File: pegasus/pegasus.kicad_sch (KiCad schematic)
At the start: 11 parts, among them IC1 Adafruit_MPL3115A2, IC2 Adafruit-BNO055-PCB, IC3 L70B-M39, IC4 RFD900, J1 Conn_01x02_Female, J2 Conn_01x02_Female, J3 Conn_01x02_Female, J4 Conn_Coaxial, J5 Conn_Coaxial, U1 Teensy4.1, U2 L7805

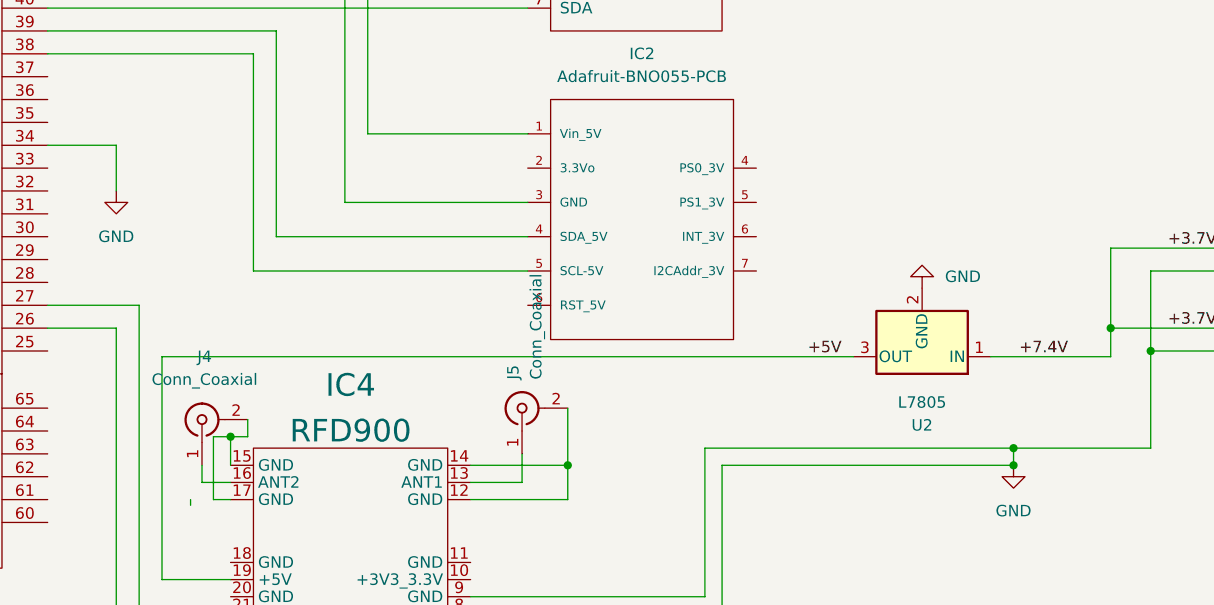
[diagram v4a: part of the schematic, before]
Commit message: added voltage regulator to schematic and pcb
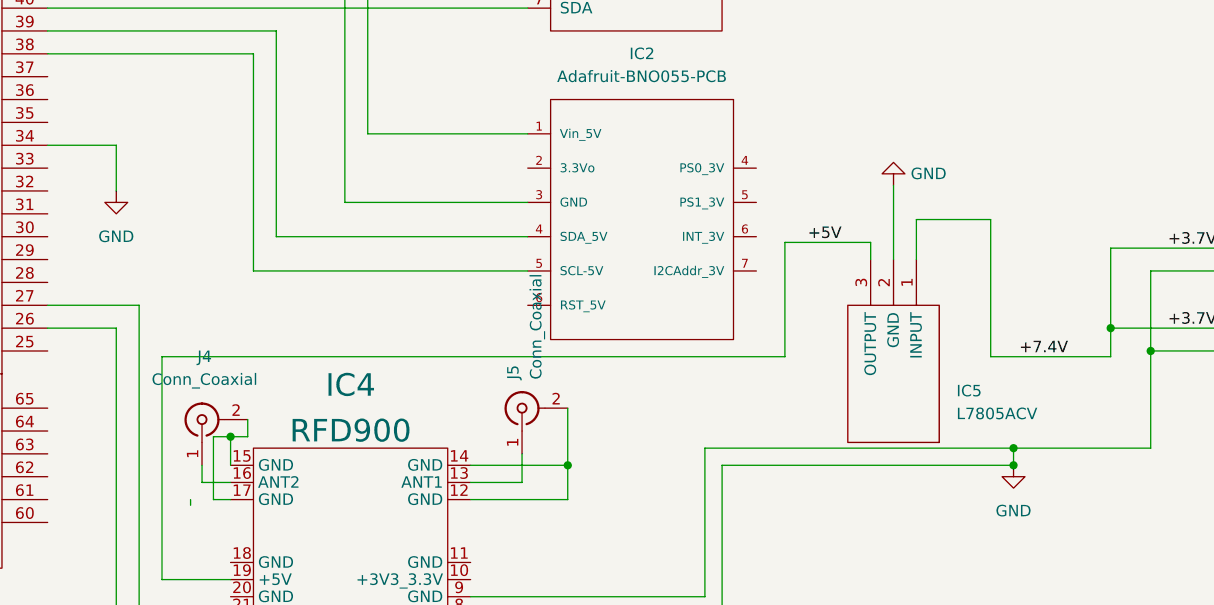
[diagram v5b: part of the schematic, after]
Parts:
- removed U2: L7805, symbol Regulator_Linear:L7805
- added IC5: L7805ACV, TO255P460X1020X2008-3P, symbol Voltage Regulator:L7805ACV
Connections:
- net +3.7V: now also IC5.1 (INPUT)
- net +5V: now also IC5.3 (OUTPUT)
- net GND: now also IC5.2 (GND)
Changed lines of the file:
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@@
   (junction (at 57.785 35.56) (diameter 0) (color 0 0 0 0)
   )
+  (wire (pts (xy 179.705 150.495) (xy 110.49 150.495))
+    (stroke (width 0) (type default) (color 0 0 0 0))
+  )
   (wire (pts (xy 105.41 127) (xy 105.41 132.08))
     (stroke (width 0) (type default) (color 0 0 0 0))
@@
     (stroke (width 0) (type default) (color 0 0 0 0))
   )
-  (wire (pts (xy 187.325 150.495) (xy 110.49 150.495))
-    (stroke (width 0) (type default) (color 0 0 0 0))
-  )
   (wire (pts (xy 228.6 147.32) (xy 215.9 147.32))
     (stroke (width 0) (type default) (color 0 0 0 0))
@@
     (stroke (width 0) (type default) (color 0 0 0 0))
   )
+  (wire (pts (xy 189.23 137.795) (xy 179.705 137.795))
+    (stroke (width 0) (type default) (color 0 0 0 0))
+  )
+  (wire (pts (xy 179.705 137.795) (xy 179.705 150.495))
+    (stroke (width 0) (type default) (color 0 0 0 0))
+  )
   (wire (pts (xy 220.345 140.97) (xy 220.345 149.86))
     (stroke (width 0) (type default) (color 0 0 0 0))
@@
     (stroke (width 0) (type default) (color 0 0 0 0))
   )
+  (wire (pts (xy 202.565 135.255) (xy 194.31 135.255))
+    (stroke (width 0) (type default) (color 0 0 0 0))
+  )
+  (wire (pts (xy 194.31 135.255) (xy 194.31 139.7))
+    (stroke (width 0) (type default) (color 0 0 0 0))
+  )
   (wire (pts (xy 170.815 160.655) (xy 205.105 160.655))
     (stroke (width 0) (type default) (color 0 0 0 0))
@@
     (stroke (width 0) (type default) (color 0 0 0 0))
   )
+  (wire (pts (xy 191.77 131.445) (xy 191.77 139.7))
+    (stroke (width 0) (type default) (color 0 0 0 0))
+  )
   (wire (pts (xy 22.86 53.34) (xy 182.88 53.34))
     (stroke (width 0) (type default) (color 0 0 0 0))
@@
     (stroke (width 0) (type default) (color 0 0 0 0))
   )
+  (wire (pts (xy 189.23 139.7) (xy 189.23 137.795))
+    (stroke (width 0) (type default) (color 0 0 0 0))
+  )
   (wire (pts (xy 119.38 68.58) (xy 119.38 96.52))
     (stroke (width 0) (type default) (color 0 0 0 0))
@@
   )
   (wire (pts (xy 41.91 35.56) (xy 44.45 35.56))
+    (stroke (width 0) (type default) (color 0 0 0 0))
+  )
+  (wire (pts (xy 202.565 150.495) (xy 202.565 135.255))
     (stroke (width 0) (type default) (color 0 0 0 0))
   )
@@
     (effects (font (size 1.27 1.27)) (justify right bottom))
   )
-  (label "+5V" (at 182.245 150.495 0)
-    (effects (font (size 1.27 1.27)) (justify left bottom))
-  )
   (label "+3.7V" (at 222.25 147.32 0)
     (effects (font (size 1.27 1.27)) (justify left bottom))
   )
   (label "+3.7V" (at 222.25 138.43 0)
+    (effects (font (size 1.27 1.27)) (justify left bottom))
+  )
+  (label "+5V" (at 182.245 137.795 0)
     (effects (font (size 1.27 1.27)) (justify left bottom))
   )
@@
     (pin "7")
   )
-  (symbol (lib_id "power:GND") (at 194.945 142.875 180) (unit 1)
-    (in_bom yes) (on_board yes) (fields_autoplaced)
-    (property "Reference" "#PWR0105" (id 0) (at 194.945 136.525 0)
-      (effects (font (size 1.27 1.27)) hide)
-    )
-    (property "Value" "GND" (id 1) (at 197.485 141.6049 0)
+  (symbol (lib_id "power:GND") (at 191.77 131.445 180) (unit 1)
+    (in_bom yes) (on_board yes) (fields_autoplaced)
+    (property "Reference" "#PWR0105" (id 0) (at 191.77 125.095 0)
+      (effects (font (size 1.27 1.27)) hide)
+    )
+    (property "Value" "GND" (id 1) (at 193.675 130.1749 0)
       (effects (font (size 1.27 1.27)) (justify right))
     )
-    (property "Footprint" "" (id 2) (at 194.945 142.875 0)
-      (effects (font (size 1.27 1.27)) hide)
-    )
-    (property "Datasheet" "" (id 3) (at 194.945 142.875 0)
+    (property "Footprint" "" (id 2) (at 191.77 131.445 0)
+      (effects (font (size 1.27 1.27)) hide)
+    )
+    (property "Datasheet" "" (id 3) (at 191.77 131.445 0)
       (effects (font (size 1.27 1.27)) hide)
     )
@@
     (pin "2")
   )
-  (symbol (lib_id "Regulator_Linear:L7805") (at 194.945 150.495 180) (unit 1)
-    (in_bom yes) (on_board yes) (fields_autoplaced)
-    (property "Reference" "U2" (id 0) (at 194.945 158.115 0))
-    (property "Value" "L7805" (id 1) (at 194.945 155.575 0))
-    (property "Footprint" "" (id 2) (at 194.31 146.685 0)
-      (effects (font (size 1.27 1.27) italic) (justify left) hide)
-    )
-    (property "Datasheet" "http://www.st.com/content/ccc/resource/technical/document/datasheet/41/4f/b3/b0/12/d4/47/88/CD00000444.pdf/files/CD00000444.pdf/jcr:content/translations/en.CD00000444.pdf" (id 3) (at 194.945 149.225 0)
-      (effects (font (size 1.27 1.27)) hide)
+  (symbol (lib_id "Voltage Regulator:L7805ACV") (at 194.31 139.7 180) (unit 1)
+    (in_bom yes) (on_board yes)
+    (property "Reference" "IC5" (id 0) (at 198.755 154.305 0)
+      (effects (font (size 1.27 1.27)) (justify right))
+    )
+    (property "Value" "L7805ACV" (id 1) (at 198.755 156.845 0)
+      (effects (font (size 1.27 1.27)) (justify right))
+    )
+    (property "Footprint" "TO255P460X1020X2008-3P" (id 2) (at 185.42 160.02 0)
+      (effects (font (size 1.27 1.27)) (justify left) hide)
+    )
+    (property "Datasheet" "http://uk.rs-online.com/web/p/products/2988508P" (id 3) (at 185.42 157.48 0)
+      (effects (font (size 1.27 1.27)) (justify left) hide)
+    )
+    (property "Description" "Linear voltage regulator,L7805ACV 5V 1A STMicroelectronics L7805ACV, Single Linear Voltage Regulator, 1A 5 V, 2%, 3-Pin TO-220" (id 4) (at 185.42 154.94 0)
+      (effects (font (size 1.27 1.27)) (justify left) hide)
+    )
+    (property "Height" "4.6" (id 5) (at 185.42 152.4 0)
+      (effects (font (size 1.27 1.27)) (justify left) hide)
+    )
+    (property "RS Part Number" "2988508P" (id 6) (at 185.42 149.86 0)
+      (effects (font (size 1.27 1.27)) (justify left) hide)
+    )
+    (property "RS Price/Stock" "http://uk.rs-online.com/web/p/products/2988508P" (id 7) (at 185.42 147.32 0)
+      (effects (font (size 1.27 1.27)) (justify left) hide)
+    )
+    (property "Manufacturer_Name" "STMicroelectronics" (id 8) (at 185.42 144.78 0)
+      (effects (font (size 1.27 1.27)) (justify left) hide)
+    )
+    (property "Manufacturer_Part_Number" "L7805ACV" (id 9) (at 185.42 142.24 0)
+      (effects (font (size 1.27 1.27)) (justify left) hide)
+    )
+    (property "Allied_Number" "70013701" (id 10) (at 185.42 139.7 0)
+      (effects (font (size 1.27 1.27)) (justify left) hide)
     )
     (pin "1")
@@
       (reference "#PWR0104") (unit 1) (value "GND") (footprint "")
     )
-    (path "/353c06e4-c9fb-41ac-9555-97e46d89901c"
+    (path "/2633f538-169e-402e-aae6-8b6c4ee49d73"
       (reference "#PWR0105") (unit 1) (value "GND") (footprint "")
     )
@@
       (reference "IC4") (unit 1) (value "RFD900") (footprint "RFD900:1x28")
     )
+    (path "/57cb0745-7118-4f35-b7ad-15a440e8d2d7"
+      (reference "IC5") (unit 1) (value "L7805ACV") (footprint "TO255P460X1020X2008-3P")
+    )
     (path "/50f78511-b951-4dcf-a410-ebb84e2ce437"
       (reference "J1") (unit 1) (value "Conn_01x02_Female") (footprint "Connector_PinHeader_2.00mm:PinHeader_1x02_P2.00mm_Vertical")
@@
       (reference "U1") (unit 1) (value "Teensy4.1") (footprint "Teensy_4.1:Teensy_4.1")
     )
-    (path "/52b10da1-d858-4a3b-b810-cb4019703dd8"
-      (reference "U2") (unit 1) (value "L7805") (footprint "")
-    )
-  )
+  )
